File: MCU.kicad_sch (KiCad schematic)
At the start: 43 parts, among them J301 SWD, J302 USB4110-GF-A_REVB, SW301 SW_SPDT, U301 STM32F405RGT6, U302 USBLC6-2SC6, Y301 16MHz

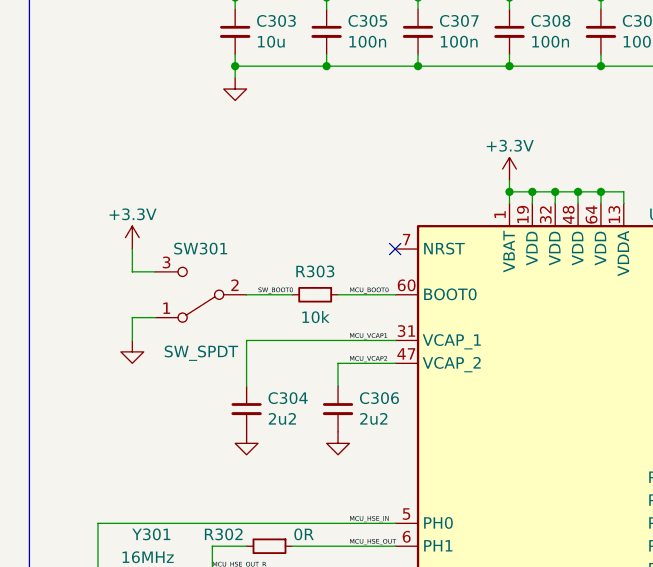
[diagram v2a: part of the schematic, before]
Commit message: incorporated rework into official design
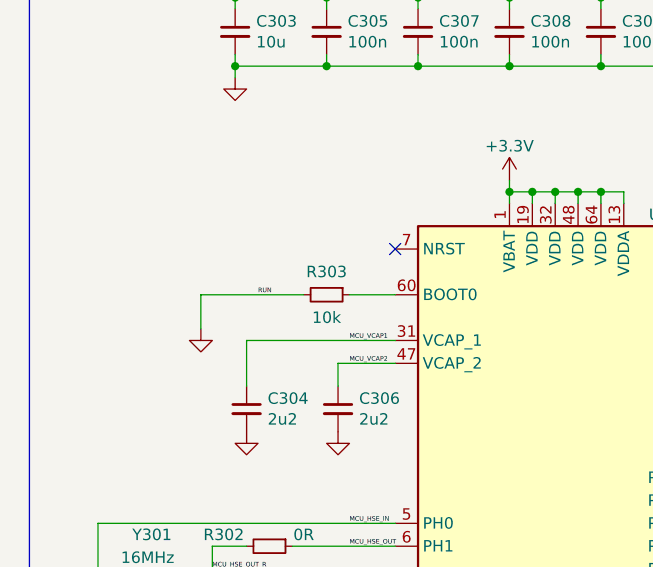
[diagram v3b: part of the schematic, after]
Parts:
- removed SW301: SW_SPDT, Button_Switch_SMD:SW_SPDT_PCM12, symbol Switch:SW_SPDT
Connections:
- net SW_BOOT0 is gone; now on net GND: R303.2
- net MCU_BOOT0: no longer names the net of R303.1, U301.60 (BOOT0)
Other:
- moved on the sheet: R303
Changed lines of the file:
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@@
     (stroke (width 0) (type default) (color 0 0 0 0))
   )
-  (wire (pts (xy 49.53 83.82) (xy 54.61 83.82))
+  (wire (pts (xy 44.45 83.82) (xy 55.88 83.82))
     (stroke (width 0) (type default) (color 0 0 0 0))
   )
@@
     (stroke (width 0) (type default) (color 0 0 0 0))
   )
-  (wire (pts (xy 36.83 81.28) (xy 39.37 81.28))
-    (stroke (width 0) (type default) (color 0 0 0 0))
-  )
   (wire (pts (xy 101.6 149.86) (xy 123.19 149.86))
     (stroke (width 0) (type default) (color 0 0 0 0))
@@
     (stroke (width 0) (type default) (color 0 0 0 0))
   )
-  (wire (pts (xy 36.83 86.36) (xy 39.37 86.36))
-    (stroke (width 0) (type default) (color 0 0 0 0))
-  )
   (wire (pts (xy 205.74 46.99) (xy 203.2 46.99))
     (stroke (width 0) (type default) (color 0 0 0 0))
@@
     (stroke (width 0) (type default) (color 0 0 0 0))
   )
-  (wire (pts (xy 36.83 88.9) (xy 36.83 86.36))
-    (stroke (width 0) (type default) (color 0 0 0 0))
-  )
   (wire (pts (xy 238.76 39.37) (xy 248.92 39.37))
     (stroke (width 0) (type default) (color 0 0 0 0))
@@
     (stroke (width 0) (type default) (color 0 0 0 0))
   )
-  (wire (pts (xy 36.83 78.74) (xy 36.83 81.28))
-    (stroke (width 0) (type default) (color 0 0 0 0))
-  )
   (wire (pts (xy 40.64 121.92) (xy 40.64 128.27))
     (stroke (width 0) (type default) (color 0 0 0 0))
@@
     (stroke (width 0) (type default) (color 0 0 0 0))
   )
+  (wire (pts (xy 44.45 87.63) (xy 44.45 83.82))
+    (stroke (width 0) (type default) (color 0 0 0 0))
+  )
   (wire (pts (xy 259.08 41.91) (xy 254 41.91))
     (stroke (width 0) (type default) (color 0 0 0 0))
@@
     (stroke (width 0) (type default) (color 0 0 0 0))
   )
-  (wire (pts (xy 59.69 83.82) (xy 66.04 83.82))
+  (wire (pts (xy 60.96 83.82) (xy 66.04 83.82))
     (stroke (width 0) (type default) (color 0 0 0 0))
   )
@@
     (effects (font (size 1.27 1.27)) (justify left bottom))
   )
-  (label "MCU_BOOT0" (at 60.96 83.82 0)
-    (effects (font (size 0.508 0.508)) (justify left bottom))
-  )
   (label "MCU_VCAP2" (at 60.96 91.44 0)
     (effects (font (size 0.508 0.508)) (justify left bottom))
@@
     (effects (font (size 0.508 0.508)) (justify left bottom))
   )
-  (label "SW_BOOT0" (at 50.8 83.82 0)
+  (label "RUN" (at 50.8 83.82 0)
     (effects (font (size 0.508 0.508)) (justify left bottom))
   )
@@
     (pin "1")
   )
-  (symbol (lib_id "Switch:SW_SPDT") (at 44.45 83.82 180) (unit 1)
-    (in_bom yes) (on_board yes)
-    (property "Reference" "SW301" (id 0) (at 44.45 78.74 0))
-    (property "Value" "SW_SPDT" (id 1) (at 44.45 90.17 0))
-    (property "Footprint" "Button_Switch_SMD:SW_SPDT_PCM12" (id 2) (at 44.45 83.82 0)
-      (effects (font (size 1.27 1.27)) hide)
-    )
-    (property "Datasheet" "~" (id 3) (at 44.45 83.82 0)
-      (effects (font (size 1.27 1.27)) hide)
-    )
-    (property "LCSC Part #" "C431541" (id 4) (at 44.45 83.82 0)
-      (effects (font (size 1.27 1.27)) hide)
-    )
-    (pin "1")
-    (pin "2")
-    (pin "3")
-  )
-  (symbol (lib_id "Device:R_Small") (at 57.15 83.82 270) (unit 1)
-    (in_bom yes) (on_board yes)
-    (property "Reference" "R303" (id 0) (at 57.15 81.28 90))
-    (property "Value" "10k" (id 1) (at 57.15 86.36 90))
-    (property "Footprint" "Resistor_SMD:R_0402_1005Metric" (id 2) (at 57.15 83.82 0)
-      (effects (font (size 1.27 1.27)) hide)
-    )
-    (property "Datasheet" "~" (id 3) (at 57.15 83.82 0)
-      (effects (font (size 1.27 1.27)) hide)
-    )
-    (property "LCSC Part #" "C25744" (id 4) (at 57.15 83.82 0)
-      (effects (font (size 1.27 1.27)) hide)
-    )
-    (pin "1")
-    (pin "2")
-  )
-  (symbol (lib_id "power:GND") (at 36.83 88.9 0) (unit 1)
-    (in_bom yes) (on_board yes)
-    (property "Reference" "#PWR0302" (id 0) (at 36.83 95.25 0)
-      (effects (font (size 1.27 1.27)) hide)
-    )
-    (property "Value" "GND" (id 1) (at 36.83 92.71 0)
-      (effects (font (size 1.27 1.27)) hide)
-    )
-    (property "Footprint" "" (id 2) (at 36.83 88.9 0)
-      (effects (font (size 1.27 1.27)) hide)
-    )
-    (property "Datasheet" "" (id 3) (at 36.83 88.9 0)
-      (effects (font (size 1.27 1.27)) hide)
-    )
-    (pin "1")
-  )
-  (symbol (lib_id "BluePhil-rescue:+3.3V-power") (at 36.83 78.74 0) (unit 1)
-    (in_bom yes) (on_board yes)
-    (property "Reference" "#PWR0301" (id 0) (at 36.83 82.55 0)
-      (effects (font (size 1.27 1.27)) hide)
-    )
-    (property "Value" "+3.3V" (id 1) (at 36.83 74.93 0))
-    (property "Footprint" "" (id 2) (at 36.83 78.74 0)
-      (effects (font (size 1.27 1.27)) hide)
-    )
-    (property "Datasheet" "" (id 3) (at 36.83 78.74 0)
-      (effects (font (size 1.27 1.27)) hide)
-    )
-    (pin "1")
+  (symbol (lib_id "Device:R_Small") (at 58.42 83.82 270) (unit 1)
+    (in_bom yes) (on_board yes)
+    (property "Reference" "R303" (id 0) (at 58.42 81.28 90))
+    (property "Value" "10k" (id 1) (at 58.42 86.36 90))
+    (property "Footprint" "Resistor_SMD:R_0402_1005Metric" (id 2) (at 58.42 83.82 0)
+      (effects (font (size 1.27 1.27)) hide)
+    )
+    (property "Datasheet" "~" (id 3) (at 58.42 83.82 0)
+      (effects (font (size 1.27 1.27)) hide)
+    )
+    (property "LCSC Part #" "C25744" (id 4) (at 58.42 83.82 0)
+      (effects (font (size 1.27 1.27)) hide)
+    )
+    (pin "1")
+    (pin "2")
   )
   (symbol (lib_id "Device:Crystal_GND24_Small") (at 39.37 118.11 0) (unit 1)
@@
     (pin "2")
   )
+  (symbol (lib_id "power:GND") (at 44.45 87.63 0) (unit 1)
+    (in_bom yes) (on_board yes)
+    (property "Reference" "#PWR0101" (id 0) (at 44.45 93.98 0)
+      (effects (font (size 1.27 1.27)) hide)
+    )
+    (property "Value" "GND" (id 1) (at 44.45 91.44 0)
+      (effects (font (size 1.27 1.27)) hide)
+    )
+    (property "Footprint" "" (id 2) (at 44.45 87.63 0)
+      (effects (font (size 1.27 1.27)) hide)
+    )
+    (property "Datasheet" "" (id 3) (at 44.45 87.63 0)
+      (effects (font (size 1.27 1.27)) hide)
+    )
+    (pin "1")
+  )
   (symbol (lib_id "USB4110:USB4110-GF-A_REVB") (at 213.36 107.95 0) (unit 1)
